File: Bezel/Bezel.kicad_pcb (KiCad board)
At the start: 2 copper layers, 33.8 x 114.2 mm, 9 parts, among them U10 VDMR10A1, U11 VDMR10A1, U12 VDMR10A1, U4 VDMR10A1, U5 VDMR10A1, U6 VDMR10A1, U7 VDMR10A1, U8 VDMR10A1, U9 VDMR10A1

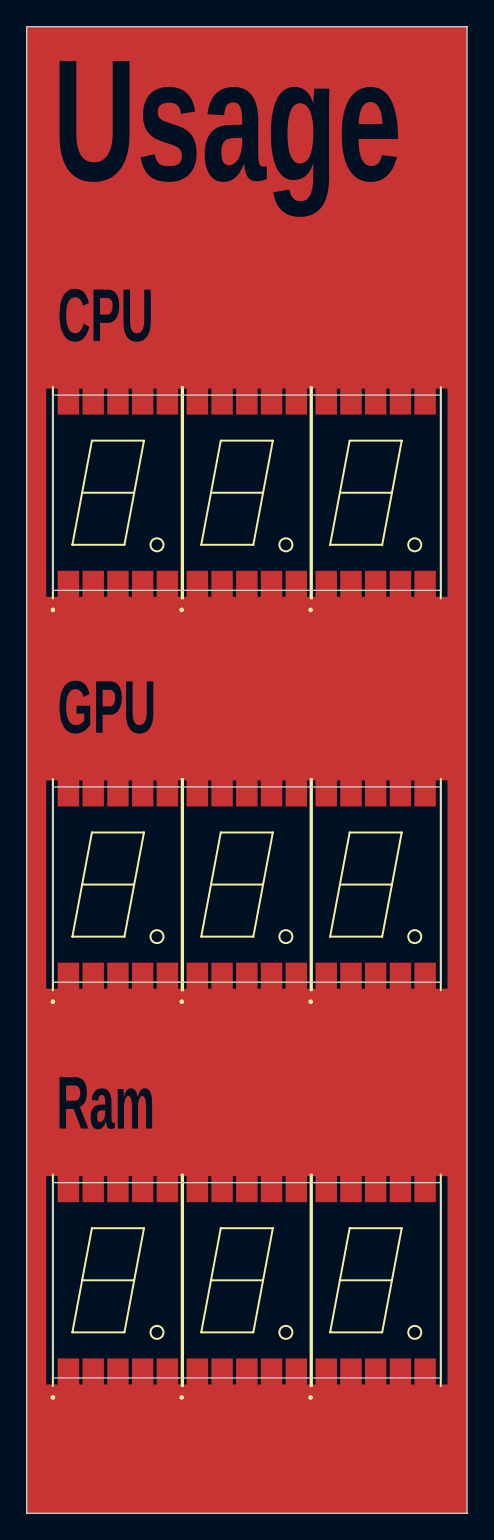
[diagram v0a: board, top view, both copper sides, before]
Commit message: Remove LED modules from Bezel PCB; generate production files
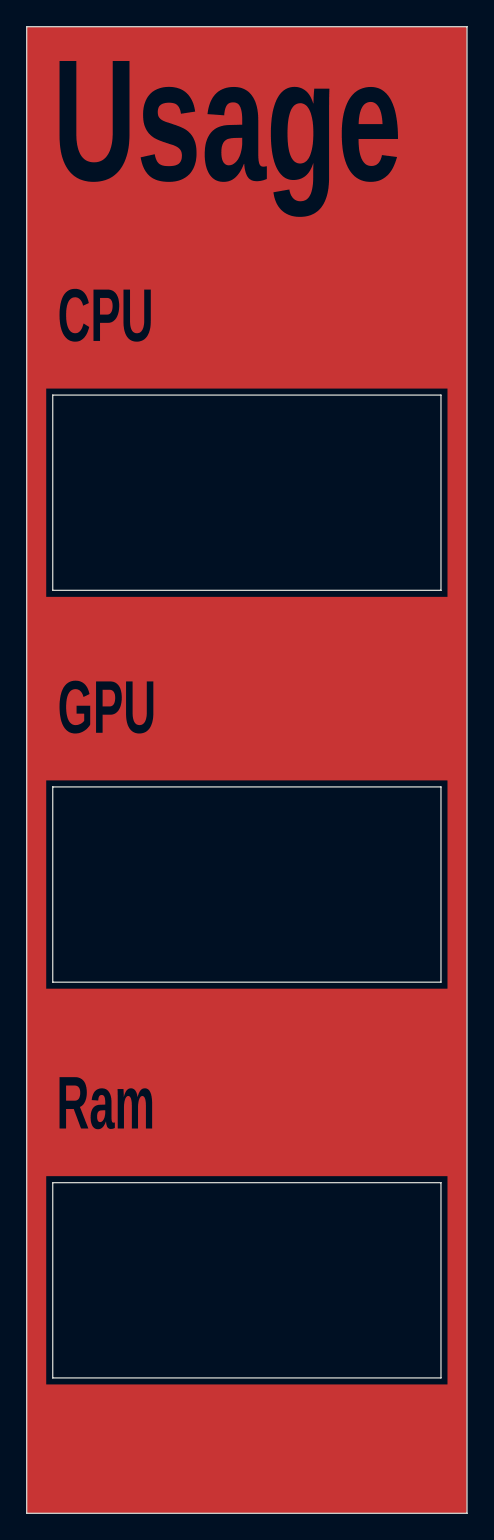
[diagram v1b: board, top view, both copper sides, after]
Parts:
- removed U10, U11, U12, U4, U5, U6, U7, U8, U9: VDMR10A1, LEDMatrix:SON_R10A1_VIS_mod_noholes
